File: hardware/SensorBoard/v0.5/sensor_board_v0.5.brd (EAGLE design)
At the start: 46.8 x 39.9 mm, 57 parts, among them J3 USB-MICROB, U1 ATMEGA328P, U2 TSL2561FN, U4 MPL115A, U5 FT231XS, U6 ADMP401, U7 SHT31-DIS, U8 MCP1703CB, U9 MCP1703CB, Y1 16MHZ

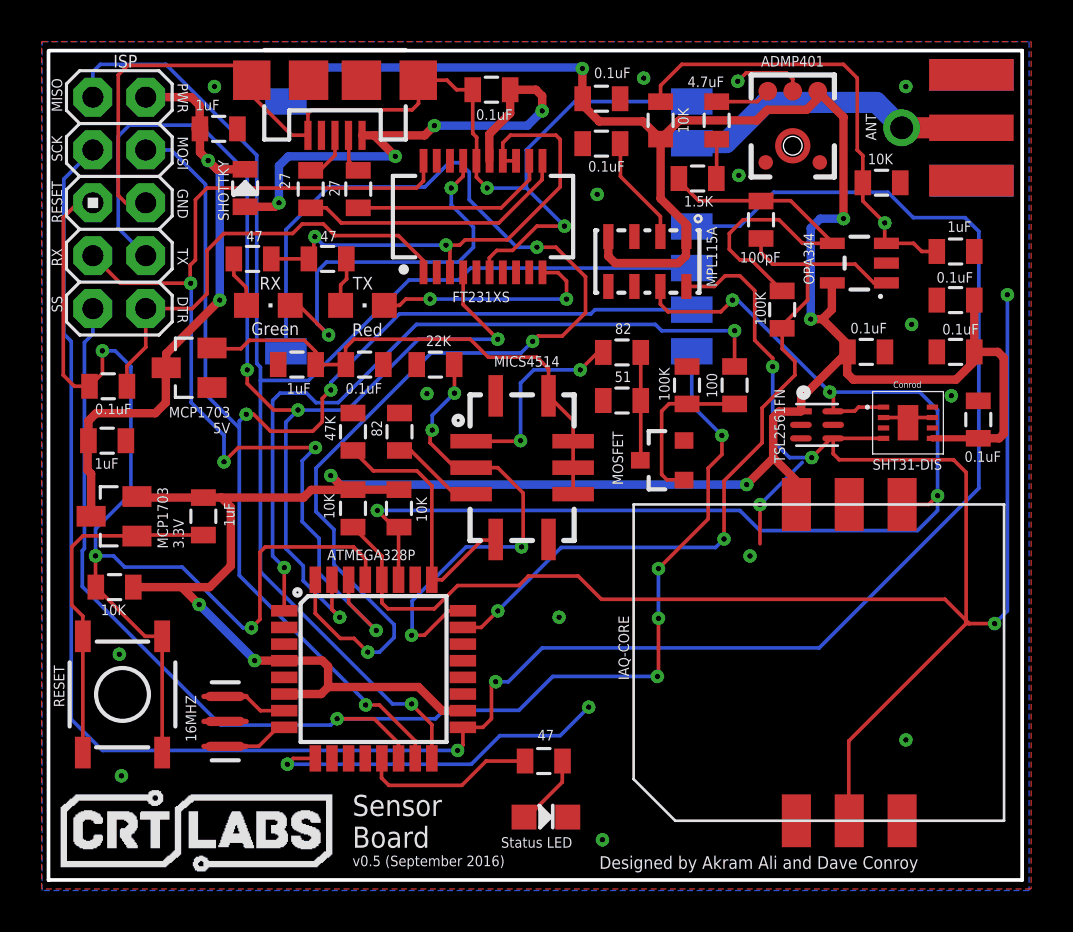
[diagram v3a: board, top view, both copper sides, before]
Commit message: Added decoupling cap for ATmega328P
0.1uF
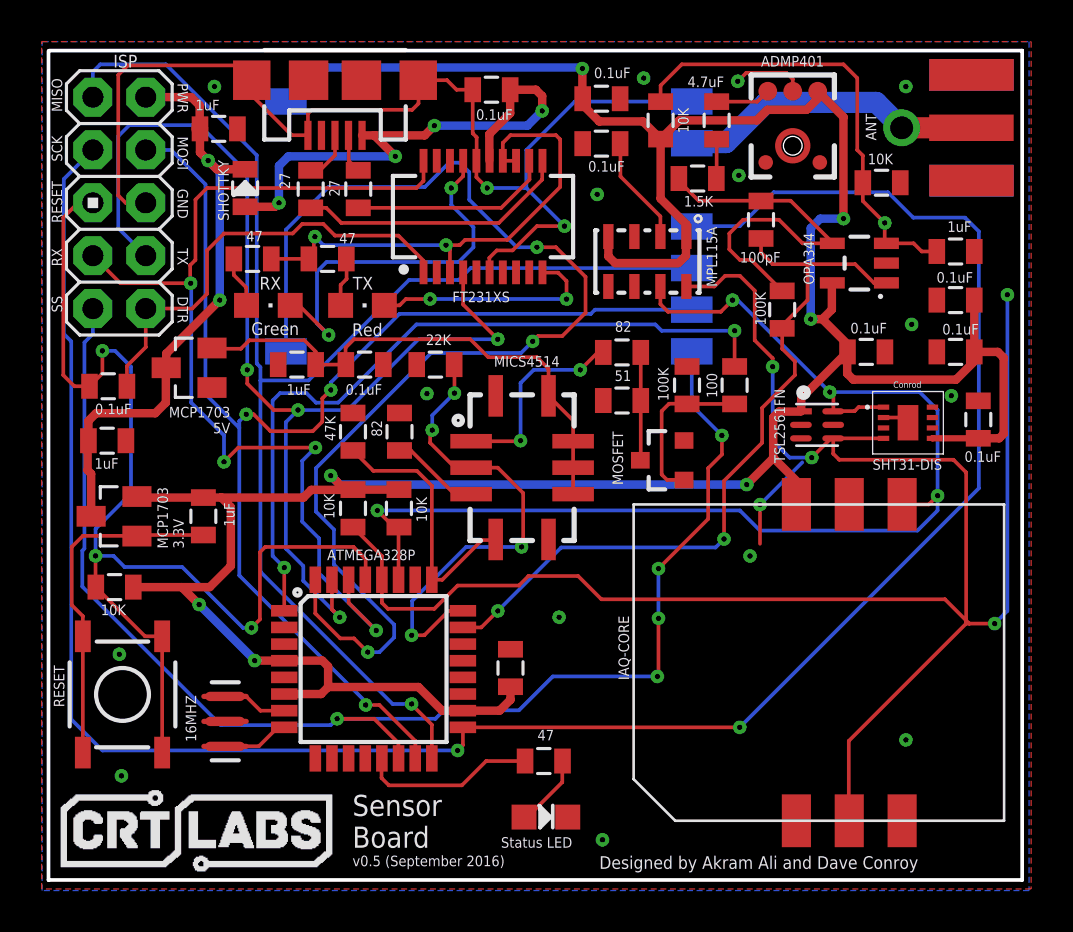
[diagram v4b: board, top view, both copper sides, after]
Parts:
- added C15: 0.1uF, SparkFun-Passives:0805
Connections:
- net GND: now also C15.2
- net VCC: now also C15.1
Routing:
- net D5: track 17.1 -> 0.00 mm, vias 2 -> 0
- net VCC: track 153.8 -> 156.9 mm
- net GND: track 81.2 -> 80.3 mm
- net SCK: track 106.6 -> 105.7 mm
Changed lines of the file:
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@@
 <attribute name="MF" value="" x="24.4856" y="31.3944" size="1.778" layer="27" display="off"/>
 <attribute name="MPN" value="" x="24.4856" y="31.3944" size="1.778" layer="27" display="off"/>
-<attribute name="VALUE" x="24.0284" y="32.2834" size="0.508" layer="121" font="vector"/>
+<attribute name="VALUE" x="24.0284" y="32.3342" size="0.508" layer="121" font="vector"/>
 </element>
 <element name="R17" library="SparkFun-Passives" package="0805" value="51" x="33.4518" y="29.6672" smashed="yes">
@@
 <attribute name="MF" value="" x="33.4518" y="29.6672" size="1.778" layer="27" display="off"/>
 <attribute name="MPN" value="" x="33.4518" y="29.6672" size="1.778" layer="27" display="off"/>
-<attribute name="VALUE" x="33.0962" y="30.5562" size="0.508" layer="121" font="vector"/>
+<attribute name="VALUE" x="33.0962" y="30.607" size="0.508" layer="121" font="vector"/>
 </element>
 <element name="R18" library="SparkFun-Passives" package="0805" value="82" x="33.4518" y="31.9786" smashed="yes" rot="R180">
@@
 <attribute name="MF" value="" x="33.4518" y="31.9786" size="1.778" layer="27" rot="R180" display="off"/>
 <attribute name="MPN" value="" x="33.4518" y="31.9786" size="1.778" layer="27" rot="R180" display="off"/>
-<attribute name="VALUE" x="33.909" y="33.3756" size="0.508" layer="121" font="vector" rot="R180"/>
+<attribute name="VALUE" x="33.909" y="33.4772" size="0.508" layer="121" font="vector" rot="R180"/>
 </element>
 <element name="R19" library="SparkFun-Passives" package="0805" value="100K" x="36.576" y="30.4038" smashed="yes" rot="R270">
@@
 <attribute name="MF" value="" x="36.576" y="30.4038" size="1.778" layer="27" rot="R270" display="off"/>
 <attribute name="MPN" value="" x="36.576" y="30.4038" size="1.778" layer="27" rot="R270" display="off"/>
-<attribute name="VALUE" x="35.7378" y="29.6418" size="0.508" layer="121" font="vector" rot="R90"/>
+<attribute name="VALUE" x="35.687" y="29.6418" size="0.508" layer="121" font="vector" rot="R90"/>
 </element>
 <element name="R20" library="SparkFun-Passives" package="0805" value="100" x="38.862" y="30.4038" smashed="yes" rot="R90">
@@
 <attribute name="OC_NEWARK" value="unknown" x="21.082" y="31.3944" size="1.778" layer="27" display="off"/>
 <attribute name="MF" value="" x="21.082" y="31.3944" size="1.778" layer="27" display="off"/>
-<attribute name="VALUE" x="20.1676" y="29.9974" size="0.508" layer="121" font="vector"/>
+<attribute name="VALUE" x="20.1676" y="29.9466" size="0.508" layer="121" font="vector"/>
 </element>
 <element name="U9" library="linear" package="SOT23" value="MCP1703CB" x="12.6492" y="31.242" smashed="yes" rot="R90">
@@
 <attribute name="MPN" value="" x="26.7208" y="28.0924" size="1.778" layer="27" rot="R180" display="off"/>
 <attribute name="OC_NEWARK" value="unknown" x="26.7208" y="28.0924" size="1.778" layer="27" rot="R180" display="off"/>
-<attribute name="VALUE" x="18.4912" y="30.5054" size="0.508" layer="121" font="vector" rot="R180"/>
+<attribute name="VALUE" x="18.4912" y="30.4546" size="0.508" layer="121" font="vector" rot="R180"/>
 </element>
 <element name="U6" library="SparkFun-Sensors" package="ADMP401" value="ADMP401" x="41.656" y="41.91" smashed="yes">
@@
 <attribute name="MPN" value="" x="19.304" y="36.4744" size="1.778" layer="27" display="off"/>
 <attribute name="OC_NEWARK" value="unknown" x="19.304" y="36.4744" size="1.778" layer="27" display="off"/>
-<attribute name="VALUE" x="18.9484" y="37.3126" size="0.508" layer="121" font="vector" rot="SR0"/>
+<attribute name="VALUE" x="19.8628" y="37.211" size="0.508" layer="121" font="vector" rot="SR0"/>
 </element>
 <element name="R11" library="SparkFun-Passives" package="0805" value="SHOTTKY" x="15.3416" y="39.878" smashed="yes" rot="R270">
@@
 <element name="X1" library="adafruit" package="SMA_EDGELAUNCH" value="" x="52.2732" y="42.7736" smashed="yes" rot="R180">
 <attribute name="VALUE" x="47.1932" y="50.3936" size="0.8128" layer="27" ratio="10"/>
+</element>
+<element name="C15" library="SparkFun-Passives" package="0805" value="0.1uF" x="28.0924" y="16.8148" smashed="yes" rot="R90">
+<attribute name="VALUE" x="29.6926" y="15.7988" size="0.508" layer="27" font="vector" rot="R90"/>
 </element>
 </elements>
@@
 <contactref element="U7" pad="PAD"/>
 <contactref element="U7" pad="P$7"/>
-<wire x1="48.3682" y1="28.8504" x2="47.4432" y2="28.8504" width="0.1778" layer="1"/>
-<wire x1="47.4432" y1="28.8504" x2="47.1932" y2="28.6004" width="0.1778" layer="1"/>
 <contactref element="U7" pad="P$2"/>
-<wire x1="46.0182" y1="28.8504" x2="46.9432" y2="28.8504" width="0.1778" layer="1"/>
 <via x="32.512" y="8.5598" extent="1-16" drill="0.254" diameter="0.127"/>
 <via x="39.5986" y="22.1996" extent="1-16" drill="0.254" diameter="0.127"/>
@@
 <via x="34.4932" y="45.1612" extent="1-16" drill="0.254" diameter="0.127"/>
 <via x="47.0916" y="44.7548" extent="1-16" drill="0.254" diameter="0.127"/>
-<wire x1="46.9432" y1="28.8504" x2="47.1932" y2="28.6004" width="0" layer="19" extent="1-1"/>
+<wire x1="46.0182" y1="28.8504" x2="46.9432" y2="28.8504" width="0.1778" layer="1"/>
+<wire x1="46.9432" y1="28.8504" x2="47.1932" y2="28.6004" width="0.1778" layer="1"/>
+<contactref element="C15" pad="2"/>
 </signal>
 <signal name="VCC">
@@
 <wire x1="50.3792" y1="32.004" x2="50.3792" y2="31.5468" width="0.4064" layer="1"/>
 <wire x1="50.3792" y1="31.5468" x2="49.5046" y2="30.6722" width="0.4064" layer="1"/>
+<contactref element="C15" pad="1"/>
+<wire x1="25.8064" y1="14.764" x2="27.5656" y2="14.764" width="0.4064" layer="1"/>
+<wire x1="27.5656" y1="14.764" x2="28.0924" y2="15.2908" width="0.4064" layer="1"/>
+<wire x1="28.0924" y1="15.2908" x2="28.0924" y2="15.9148" width="0.4064" layer="1"/>
 </signal>
 <signal name="SCL">
@@
 <signal name="D5">
 <contactref element="U1" pad="9"/>
-<wire x1="27.5844" y1="13.5636" x2="30.48" y2="13.5636" width="0.1778" layer="16"/>
-<wire x1="18.7138" y1="12.4714" x2="17.653" y2="12.4714" width="0.1778" layer="1"/>
-<wire x1="17.653" y1="12.4714" x2="17.3736" y2="12.192" width="0.1778" layer="1"/>
-<via x="17.3736" y="12.192" extent="1-16" drill="0.254" diameter="0.127"/>
-<wire x1="17.3736" y1="12.192" x2="26.2128" y2="12.192" width="0.1778" layer="16"/>
-<wire x1="26.2128" y1="12.192" x2="27.5844" y2="13.5636" width="0.1778" layer="16"/>
-<wire x1="30.48" y1="13.5636" x2="31.8516" y2="14.9352" width="0.1778" layer="16"/>
-<via x="31.8516" y="14.9352" extent="1-16" drill="0.254" diameter="0.127"/>
-<wire x1="31.8262" y1="14.9606" x2="31.8516" y2="14.9352" width="0.1778" layer="1"/>
 </signal>
 <signal name="N$4">
@@
 <wire x1="6.6294" y1="40.3098" x2="8.0264" y2="41.7068" width="0.1778" layer="16"/>
 <contactref element="U$4" pad="SCK"/>
-<wire x1="25.8064" y1="13.964" x2="26.7656" y2="13.964" width="0.1778" layer="1"/>
-<wire x1="26.7656" y1="13.964" x2="27.178" y2="14.3764" width="0.1778" layer="1"/>
-<wire x1="27.178" y1="14.3764" x2="27.178" y2="15.9512" width="0.1778" layer="1"/>
-<wire x1="27.178" y1="15.9512" x2="27.3812" y2="16.1544" width="0.1778" layer="1"/>
-<via x="27.3812" y="16.1544" extent="1-16" drill="0.254" diameter="0.127"/>
-<wire x1="27.3812" y1="16.1544" x2="27.9908" y2="16.1544" width="0.1778" layer="16"/>
-<wire x1="27.9908" y1="16.1544" x2="29.6164" y2="17.78" width="0.1778" layer="16"/>
-<wire x1="29.6164" y1="17.78" x2="42.926" y2="17.78" width="0.1778" layer="16"/>
-<wire x1="42.926" y1="17.78" x2="50.5968" y2="25.4508" width="0.1778" layer="16"/>
 <wire x1="36.7792" y1="38.0576" x2="36.8036" y2="38.0332" width="0.1778" layer="16"/>
 <wire x1="40.7416" y1="39.6748" x2="39.116" y2="38.0492" width="0.1778" layer="16"/>
@@
 <wire x1="49.9364" y1="38.4556" x2="50.5968" y2="37.7952" width="0.1778" layer="16"/>
 <wire x1="50.5968" y1="37.7952" x2="50.5968" y2="25.4508" width="0.1778" layer="16"/>
+<wire x1="25.8064" y1="13.964" x2="39.11" y2="13.964" width="0.1778" layer="1"/>
+<wire x1="39.11" y1="13.964" x2="39.116" y2="13.97" width="0.1778" layer="1"/>
+<via x="39.11" y="13.964" extent="1-16" drill="0.254" diameter="0.127"/>
+<wire x1="39.11" y1="13.964" x2="50.5968" y2="25.4508" width="0.1778" layer="16"/>
 </signal>
 <signal name="RESET">

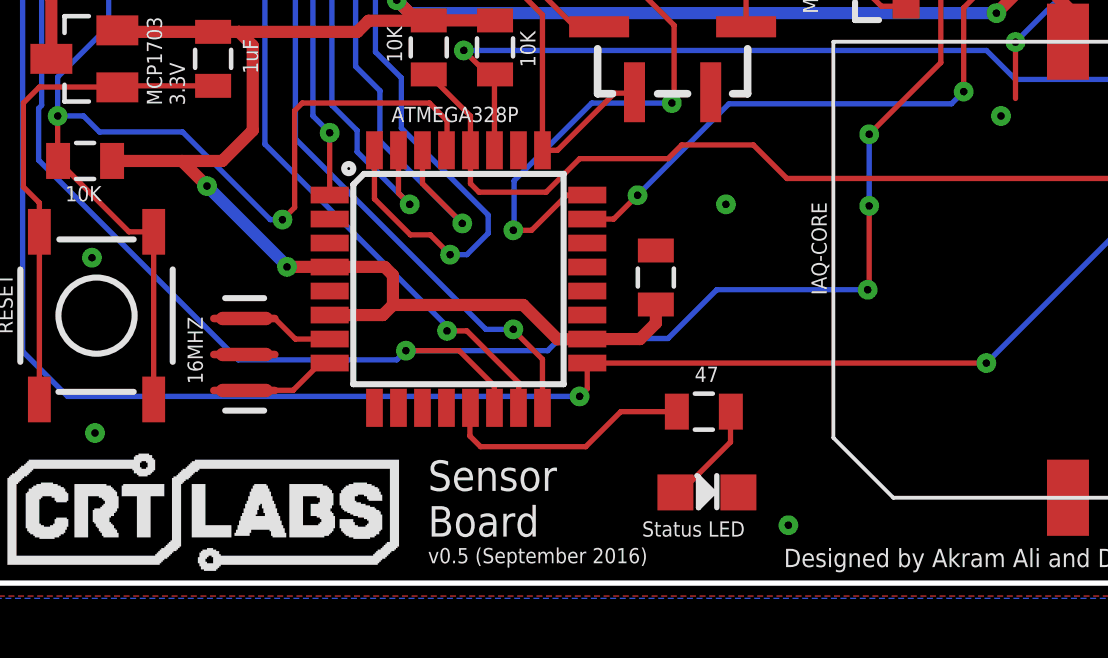
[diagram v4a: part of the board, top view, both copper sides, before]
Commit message: Rearranged status LED
and decoupling cap
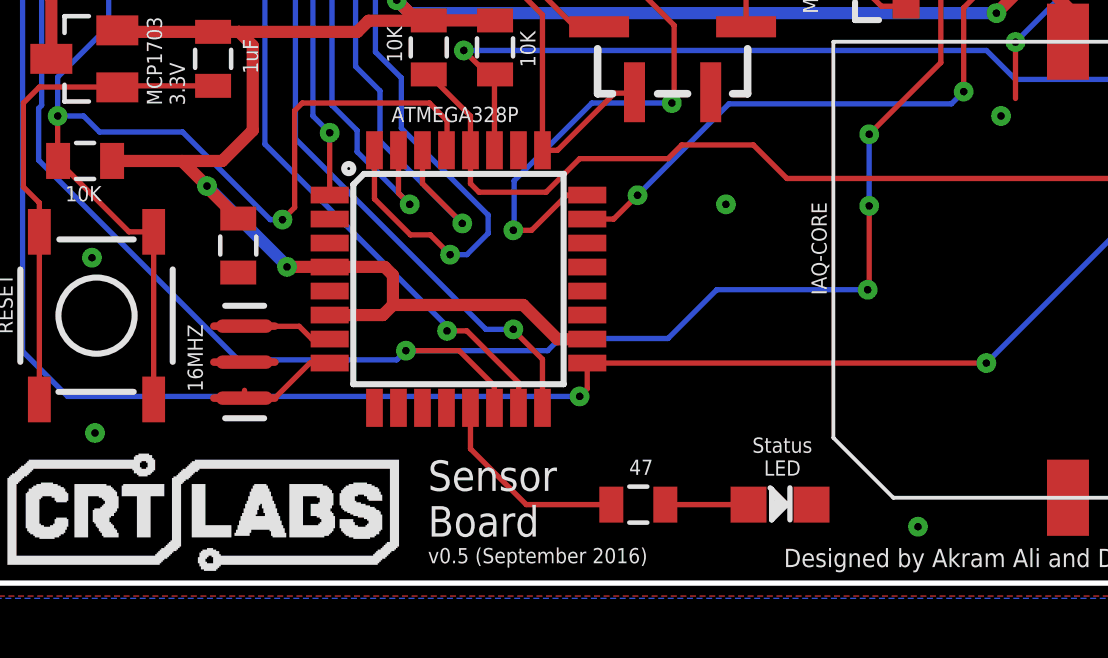
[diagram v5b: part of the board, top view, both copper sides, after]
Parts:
- moved C15 14.0 mm to (14.2, 17.9), turned to 270 degrees
- moved R4 3.79 mm to (27.5, 9.25)
- moved LED2 2.47 mm to (32.2, 9.25)
- moved Y1 0.25 mm to (14.4, 14.0)
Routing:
- net N$2: track 8.48 -> 6.86 mm
- net VCC: track 156.9 -> 155.3 mm
- net N$5: track 2.11 -> 3.02 mm
- net N$3: track 3.55 -> 2.77 mm
- net N$4: track 3.22 -> 2.57 mm

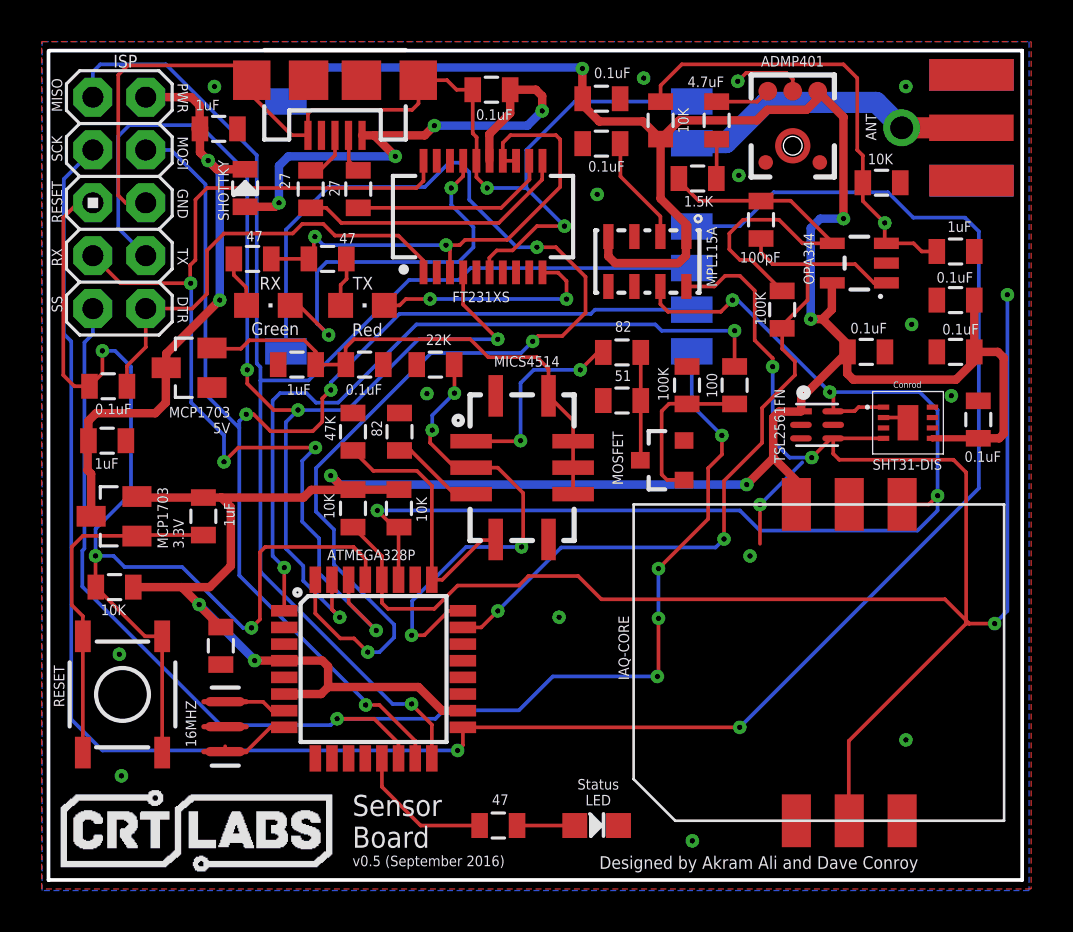
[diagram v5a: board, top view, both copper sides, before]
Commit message: Moved decoupling caps closer to ICs
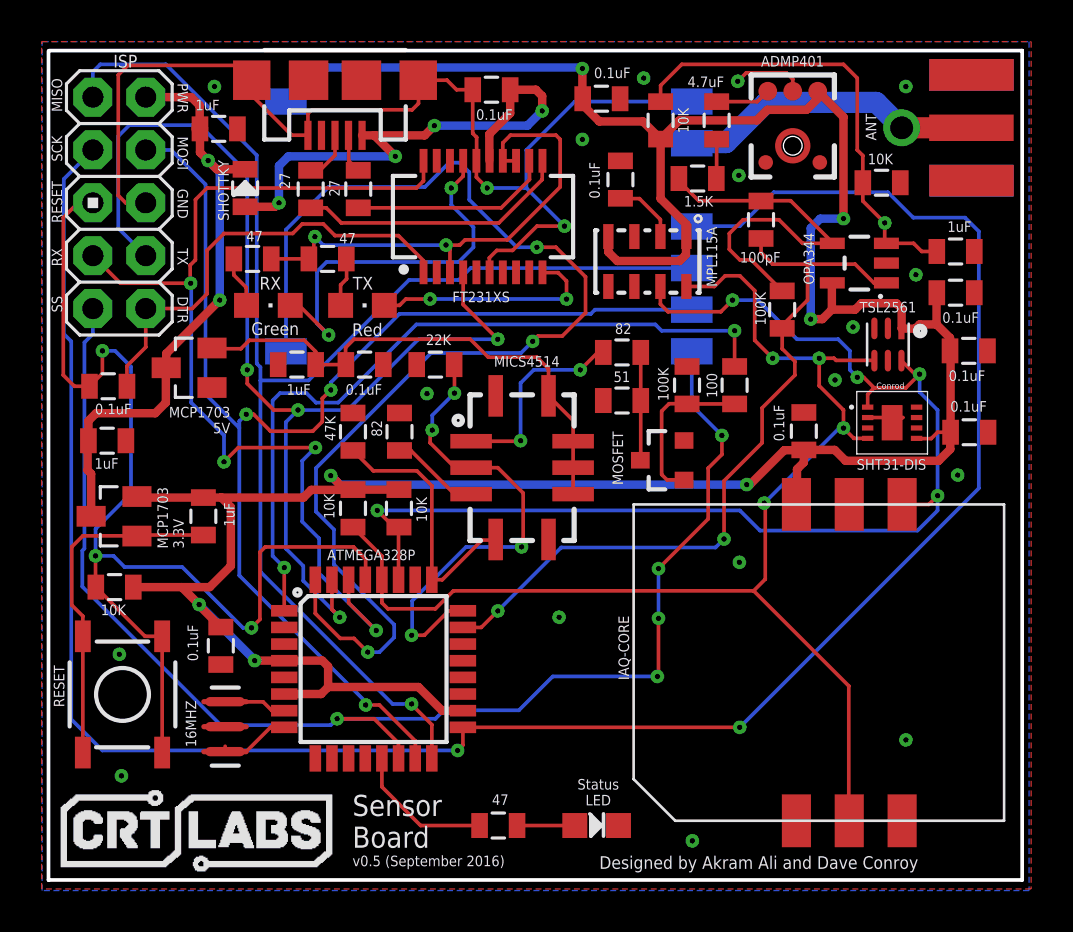
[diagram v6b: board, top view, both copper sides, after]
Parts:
- U2: value TSL2561FN -> TSL2561
- moved C5 8.40 mm to (42.2, 28.2)
- moved U2 5.15 mm to (46.2, 32.4), turned to 270 degrees
- moved C3 4.93 mm to (50.1, 32.1)
- moved C4 3.92 mm to (50.1, 28.1), turned to 0 degrees
- moved C13 1.95 mm to (33.4, 40.3), turned to 90 degrees
- moved U7 0.76 mm to (46.4, 28.6)
- moved C10 0.36 mm to (49.5, 34.8), turned to 0 degrees
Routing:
- net SCL: track 95.7 -> 62.9 mm
- net VCC: track 155.3 -> 151.4 mm
- net GND: track 80.3 -> 76.5 mm, vias 18 -> 19
- net N$12: track 5.27 -> 3.16 mm
- net SDA: track 58.7 -> 59.1 mm, vias 4 -> 5
